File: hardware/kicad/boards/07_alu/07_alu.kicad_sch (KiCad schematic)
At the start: 0 parts

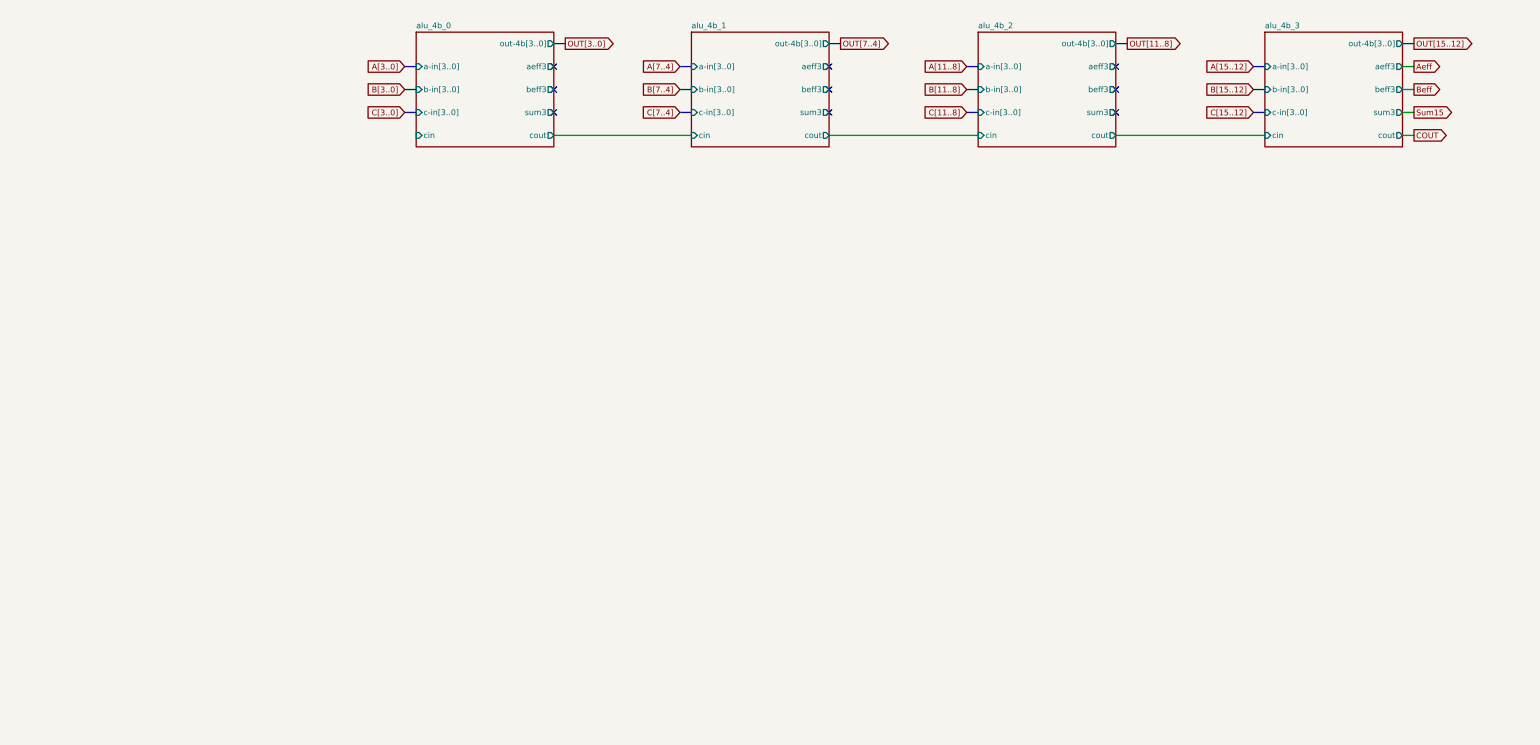
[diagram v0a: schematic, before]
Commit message: feat: implemented flag logic and led for 16 alu; refactored alu-1b cells
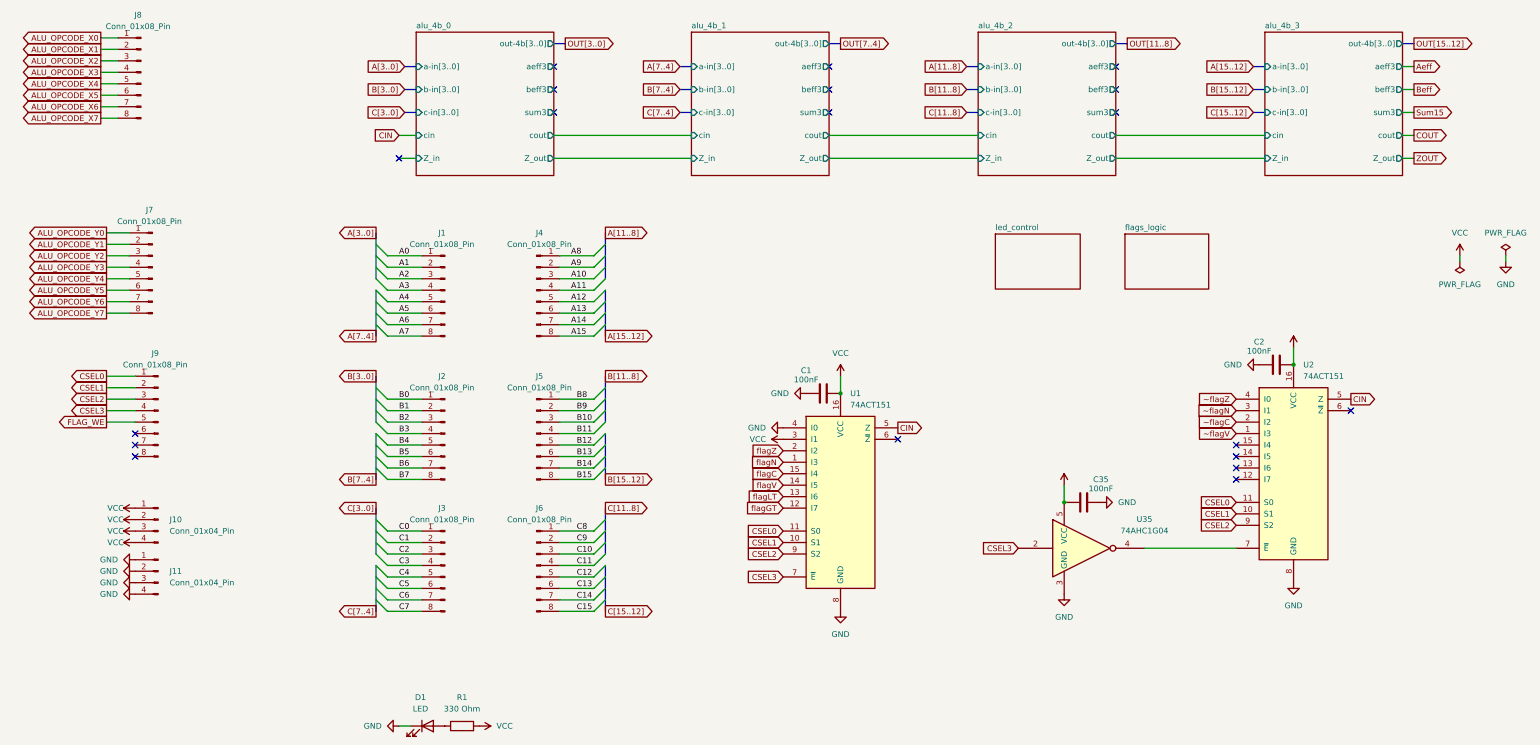
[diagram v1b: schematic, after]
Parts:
- added C1, C2, C35: 100nF, Capacitor_SMD:C_0603_1608Metric, symbol Device:C
- added D1: LED, LED_THT:LED_D5.0mm, symbol Device:LED
- added J1, J2, J3, J4, J5, J6, J7, J8, J9: Conn_01x08_Pin, Connector_PinHeader_2.54mm:PinHeader_1x08_P2.54mm_Vertical, symbol Connector:Conn_01x08_Pin
- added J10, J11: Conn_01x04_Pin, Connector_PinHeader_2.54mm:PinHeader_1x04_P2.54mm_Vertical, symbol Connector:Conn_01x04_Pin
- added R1: 330 Ohm, Resistor_SMD:R_0603_1608Metric, symbol Device:R
- added U1, U2: 74ACT151, Package_SO:SOIC-16_3.9x9.9mm_P1.27mm, symbol 74xx:74LS151
- added U35: 74AHC1G04, Package_TO_SOT_SMD:SOT-23-5, symbol 74xGxx:74AHC1G04
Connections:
- new net: D1.2 (A), R1.1
- new net: U2.7 (~{E}), U35.4
- new net A0: J1.1 (Pin_1)
- new net A1: J1.2 (Pin_2)
- new net A10: J4.3 (Pin_3)
- new net A11: J4.4 (Pin_4)
- new net A12: J4.5 (Pin_5)
- new net A13: J4.6 (Pin_6)
- new net A14: J4.7 (Pin_7)
- new net A15: J4.8 (Pin_8)
- new net A2: J1.3 (Pin_3)
- new net A3: J1.4 (Pin_4)
- new net A4: J1.5 (Pin_5)
- new net A5: J1.6 (Pin_6)
- new net A6: J1.7 (Pin_7)
- new net A7: J1.8 (Pin_8)
- new net A8: J4.1 (Pin_1)
- new net A9: J4.2 (Pin_2)
- new net ALU_OPCODE_X0: J8.1 (Pin_1)
- new net ALU_OPCODE_X1: J8.2 (Pin_2)
- new net ALU_OPCODE_X2: J8.3 (Pin_3)
- new net ALU_OPCODE_X3: J8.4 (Pin_4)
- new net ALU_OPCODE_X4: J8.5 (Pin_5)
- new net ALU_OPCODE_X5: J8.6 (Pin_6)
- new net ALU_OPCODE_X6: J8.7 (Pin_7)
- new net ALU_OPCODE_X7: J8.8 (Pin_8)
- new net ALU_OPCODE_Y0: J7.1 (Pin_1)
- new net ALU_OPCODE_Y1: J7.2 (Pin_2)
- new net ALU_OPCODE_Y2: J7.3 (Pin_3)
- new net ALU_OPCODE_Y3: J7.4 (Pin_4)
- new net ALU_OPCODE_Y4: J7.5 (Pin_5)
- new net ALU_OPCODE_Y5: J7.6 (Pin_6)
- new net ALU_OPCODE_Y6: J7.7 (Pin_7)
- new net ALU_OPCODE_Y7: J7.8 (Pin_8)
- new net B0: J2.1 (Pin_1)
- new net B1: J2.2 (Pin_2)
- new net B10: J5.3 (Pin_3)
- new net B11: J5.4 (Pin_4)
- new net B12: J5.5 (Pin_5)
- new net B13: J5.6 (Pin_6)
- new net B14: J5.7 (Pin_7)
- new net B15: J5.8 (Pin_8)
- new net B2: J2.3 (Pin_3)
- new net B3: J2.4 (Pin_4)
- new net B4: J2.5 (Pin_5)
- new net B5: J2.6 (Pin_6)
- new net B6: J2.7 (Pin_7)
- new net B7: J2.8 (Pin_8)
- new net B8: J5.1 (Pin_1)
- new net B9: J5.2 (Pin_2)
- new net C0: J3.1 (Pin_1)
- new net C1: J3.2 (Pin_2)
- new net C10: J6.3 (Pin_3)
- new net C11: J6.4 (Pin_4)
- new net C12: J6.5 (Pin_5)
- new net C13: J6.6 (Pin_6)
- new net C14: J6.7 (Pin_7)
- new net C15: J6.8 (Pin_8)
- new net C2: J3.3 (Pin_3)
- new net C3: J3.4 (Pin_4)
- new net C4: J3.5 (Pin_5)
- new net C5: J3.6 (Pin_6)
- new net C6: J3.7 (Pin_7)
- new net C7: J3.8 (Pin_8)
- new net C8: J6.1 (Pin_1)
- new net C9: J6.2 (Pin_2)
- new net CIN: U1.5 (Z), U2.5 (Z)
- new net CSEL0: J9.1 (Pin_1), U1.11 (S0), U2.11 (S0)
- new net CSEL1: J9.2 (Pin_2), U1.10 (S1), U2.10 (S1)
- new net CSEL2: J9.3 (Pin_3), U1.9 (S2), U2.9 (S2)
- new net CSEL3: J9.4 (Pin_4), U1.7 (~{E}), U35.2
- new net FLAG_WE: J9.5 (Pin_5)
- new net GND: C1.1, C2.1, C35.1, D1.1 (K), J11.1 (Pin_1), J11.2 (Pin_2), J11.3 (Pin_3), J11.4 (Pin_4), U1.4 (I0), U1.8 (GND), U2.8 (GND), U35.3 (GND)
- new net VCC: C1.2, C2.2, C35.2, J10.1 (Pin_1), J10.2 (Pin_2), J10.3 (Pin_3), J10.4 (Pin_4), R1.2, U1.16 (VCC), U1.3 (I1), U2.16 (VCC), U35.5 (VCC)
- new net flagC: U1.15 (I4)
- new net flagGT: U1.12 (I7)
- new net flagLT: U1.13 (I6)
- new net flagN: U1.1 (I3)
- new net flagV: U1.14 (I5)
- new net flagZ: U1.2 (I2)
- new net ~flagC: U2.2 (I2)
- new net ~flagN: U2.3 (I1)
- new net ~flagV: U2.1 (I3)
- new net ~flagZ: U2.4 (I0)
- no-connect marks 9 -> 19
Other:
- added sheet flags_logic (flags_logic.kicad_sch)
- added sheet led_control (led_unit.kicad_sch)
- sheet alu_4b_0 ports: added Z_in, Z_out; removed none
- sheet alu_4b_1 ports: added Z_in, Z_out; removed none
- sheet alu_4b_2 ports: added Z_in, Z_out; removed none
- sheet alu_4b_3 ports: added Z_in, Z_out; removed none

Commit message: checkpoint: most recent 16b cell: ~120mm by 120mm
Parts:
- removed C1, C2, C35: 100nF, Capacitor_SMD:C_0603_1608Metric, symbol Device:C
- removed J1, J2, J3, J4, J5, J6, J7, J8, J9: Conn_01x08_Pin, Connector_PinHeader_2.54mm:PinHeader_1x08_P2.54mm_Vertical, symbol Connector:Conn_01x08_Pin
- removed J10, J11: Conn_01x04_Pin, Connector_PinHeader_2.54mm:PinHeader_1x04_P2.54mm_Vertical, symbol Connector:Conn_01x04_Pin
- removed U1, U2: 74ACT151, Package_SO:SOIC-16_3.9x9.9mm_P1.27mm, symbol 74xx:74LS151
- removed U35: 74AHC1G04, Package_TO_SOT_SMD:SOT-23-5, symbol 74xGxx:74AHC1G04
- D1: footprint LED_THT:LED_D5.0mm -> LED_SMD:LED_0805_2012Metric
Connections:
- no-connect marks 19 -> 9
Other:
- added sheet io pins (iopins.kicad_sch)
- sheet alu_4b_0 ports: added none; removed Z_in, Z_out
- sheet alu_4b_1 ports: added none; removed Z_in, Z_out
- sheet alu_4b_2 ports: added none; removed Z_in, Z_out
- sheet alu_4b_3 ports: added none; removed Z_in, Z_out

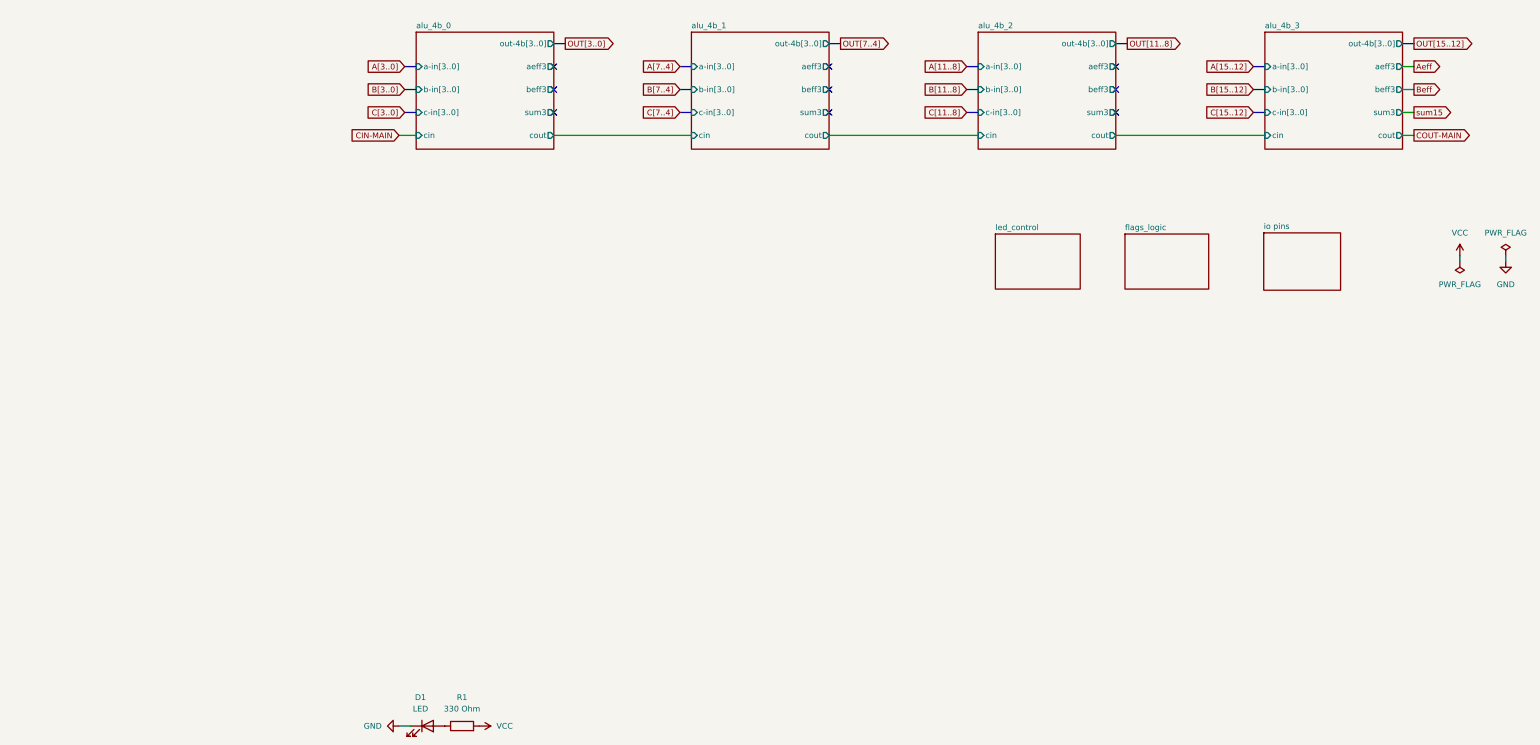
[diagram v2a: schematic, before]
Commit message: fix: resolved kicad erc tests to 0
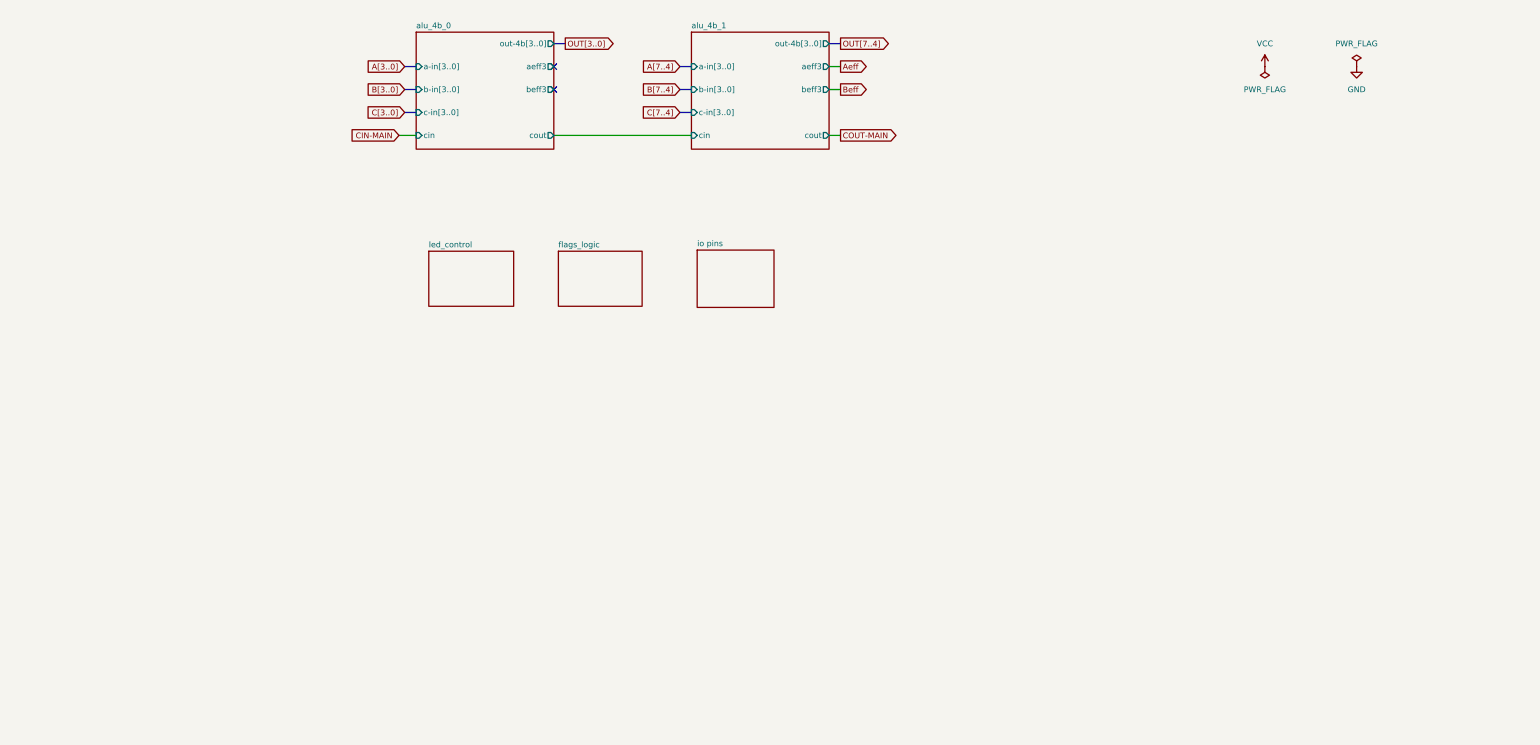
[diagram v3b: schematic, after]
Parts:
- removed D1: LED, LED_SMD:LED_0805_2012Metric, symbol Device:LED
- removed R1: 330 Ohm, Resistor_SMD:R_0603_1608Metric, symbol Device:R
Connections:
- no-connect marks 9 -> 2
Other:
- removed sheet alu_4b_2
- removed sheet alu_4b_3
- sheet alu_4b_0 ports: added none; removed sum3
- sheet alu_4b_1 ports: added none; removed sum3
